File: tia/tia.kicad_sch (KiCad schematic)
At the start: 29 parts, among them J1 ToADC, J2 Sensors, U1 Opamp_Quad, U2 Opamp_Quad, U3 MIC5366-2.0YC5-TR

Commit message: board revs, updated README
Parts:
- added C10, C11, C12, C13, C14, C15, C8, C9: 10pF, Capacitor_SMD:C_0805_2012Metric, symbol Device:C_Small
- added C7: 0.01uF X7R, Capacitor_SMD:C_0805_2012Metric, symbol Device:C_Small
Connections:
- net A0N: now also J1.1 (Pin_1), C8.2; no longer J1.2 (Pin_2)
- net A1N: now also J1.3 (Pin_3), C10.2; no longer J1.4 (Pin_4)
- net A2N: now also J1.5 (Pin_5), C12.2; no longer J1.6 (Pin_6)
- net A3N: now also J1.7 (Pin_7), C14.2; no longer J1.8 (Pin_8)
- net A4N: now also J1.9 (Pin_9), C9.2; no longer J1.10 (Pin_10)
- net A5N: now also J1.11 (Pin_11), C11.2; no longer J1.12 (Pin_12)
- net A6N: now also J1.13 (Pin_13), C13.2; no longer J1.14 (Pin_14)
- net A7N: now also J1.15 (Pin_15), C15.2; no longer J1.16 (Pin_16)
- net GND: now also J1.18 (Pin_18), J1.20 (Pin_20), C7.2; no longer J1.17 (Pin_17), J1.19 (Pin_19)
- net S0: now also C8.1
- net S1: now also C10.1
- net S2: now also C12.1
- net S3: now also C14.1
- net S4: now also C9.1
- net S5: now also C11.1
- net S6: now also C13.1
- net S7: now also C15.1
- net VAA: now also J1.19 (Pin_19); no longer J1.20 (Pin_20)
- net VREF: now also J1.10 (Pin_10), J1.12 (Pin_12), J1.14 (Pin_14), J1.16 (Pin_16), J1.17 (Pin_17), J1.2 (Pin_2), J1.4 (Pin_4), J1.6 (Pin_6), J1.8 (Pin_8); no longer J1.1 (Pin_1), J1.11 (Pin_11), J1.13 (Pin_13), J1.15 (Pin_15), J1.18 (Pin_18), J1.3 (Pin_3), J1.5 (Pin_5), J1.7 (Pin_7), J1.9 (Pin_9)
- net at U3.4 (BYP): now also C7.1
- no-connect marks 1 -> 0
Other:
- note added: "Also: REF3312AIDCKR 1.25V, lower noise $1.76/ea @ 10 NOT COMPATIBLE"
- note added: "Also: TPS717 is compatible, and can use the bypass cap"
- note removed: "Also: REF3312AIDCKR 1.25V, lower noise $1.76/ea @ 10"
- moved on the sheet: C1, C6, H1, H2, J2, R1, R2, R3, R4, R5, R6, R7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

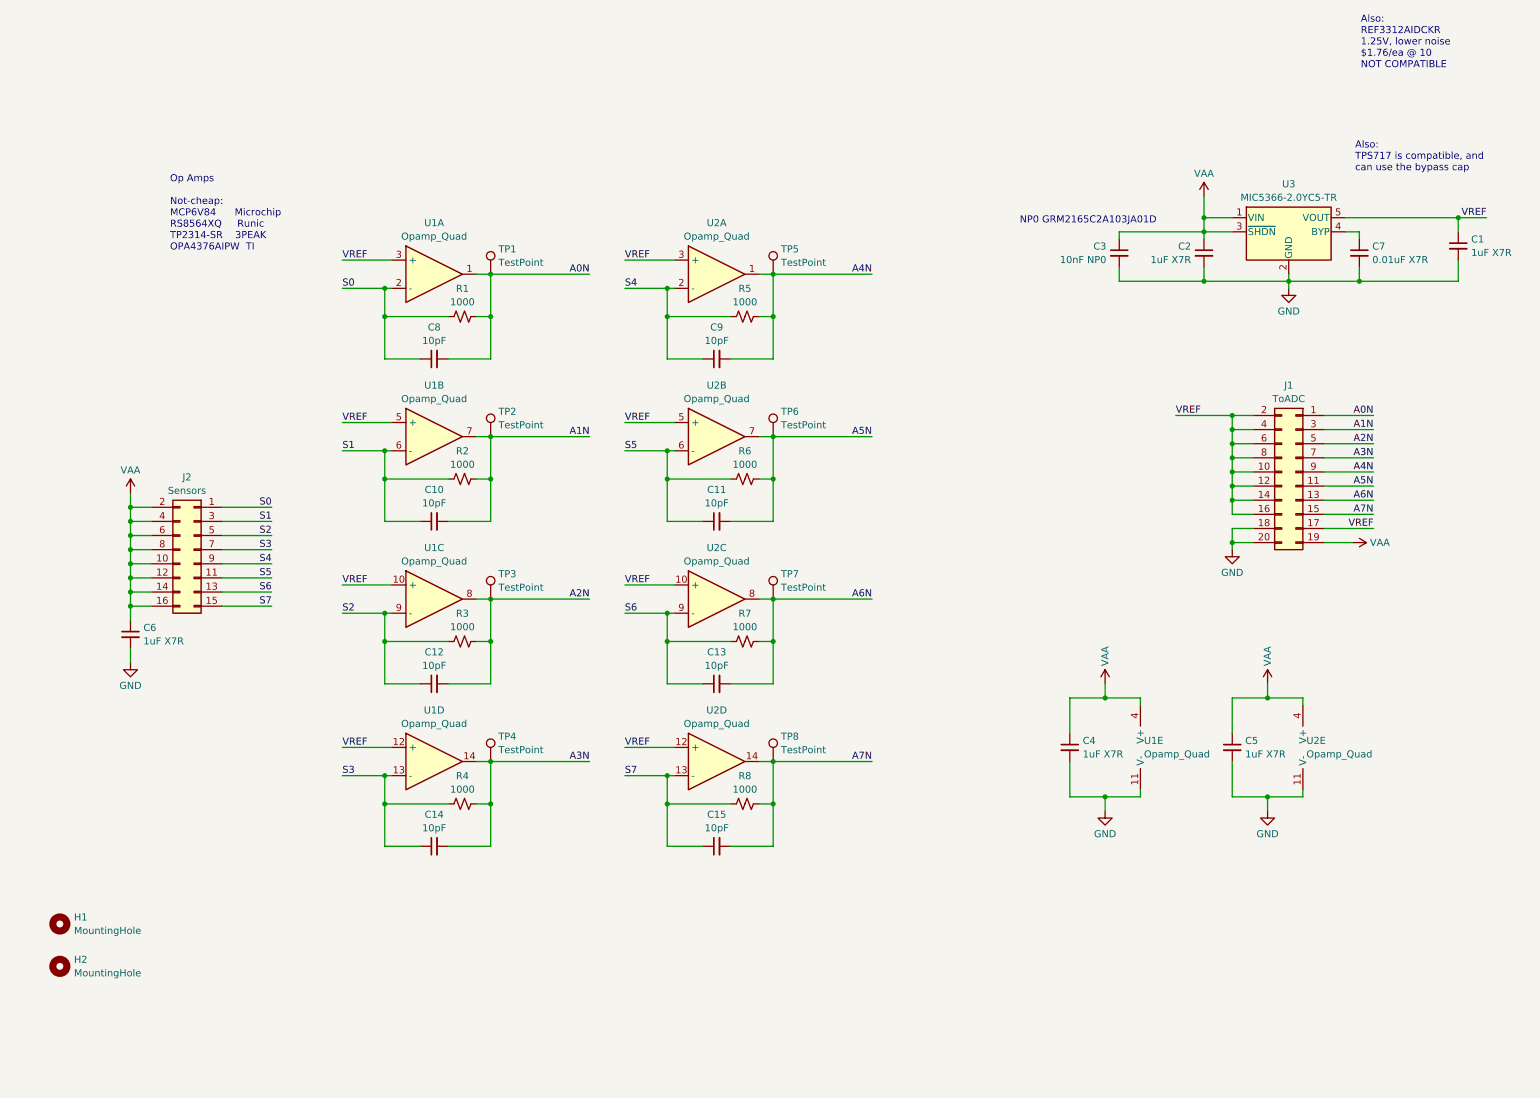
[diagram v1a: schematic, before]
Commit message: rev2 of tia board, with bias and LPF
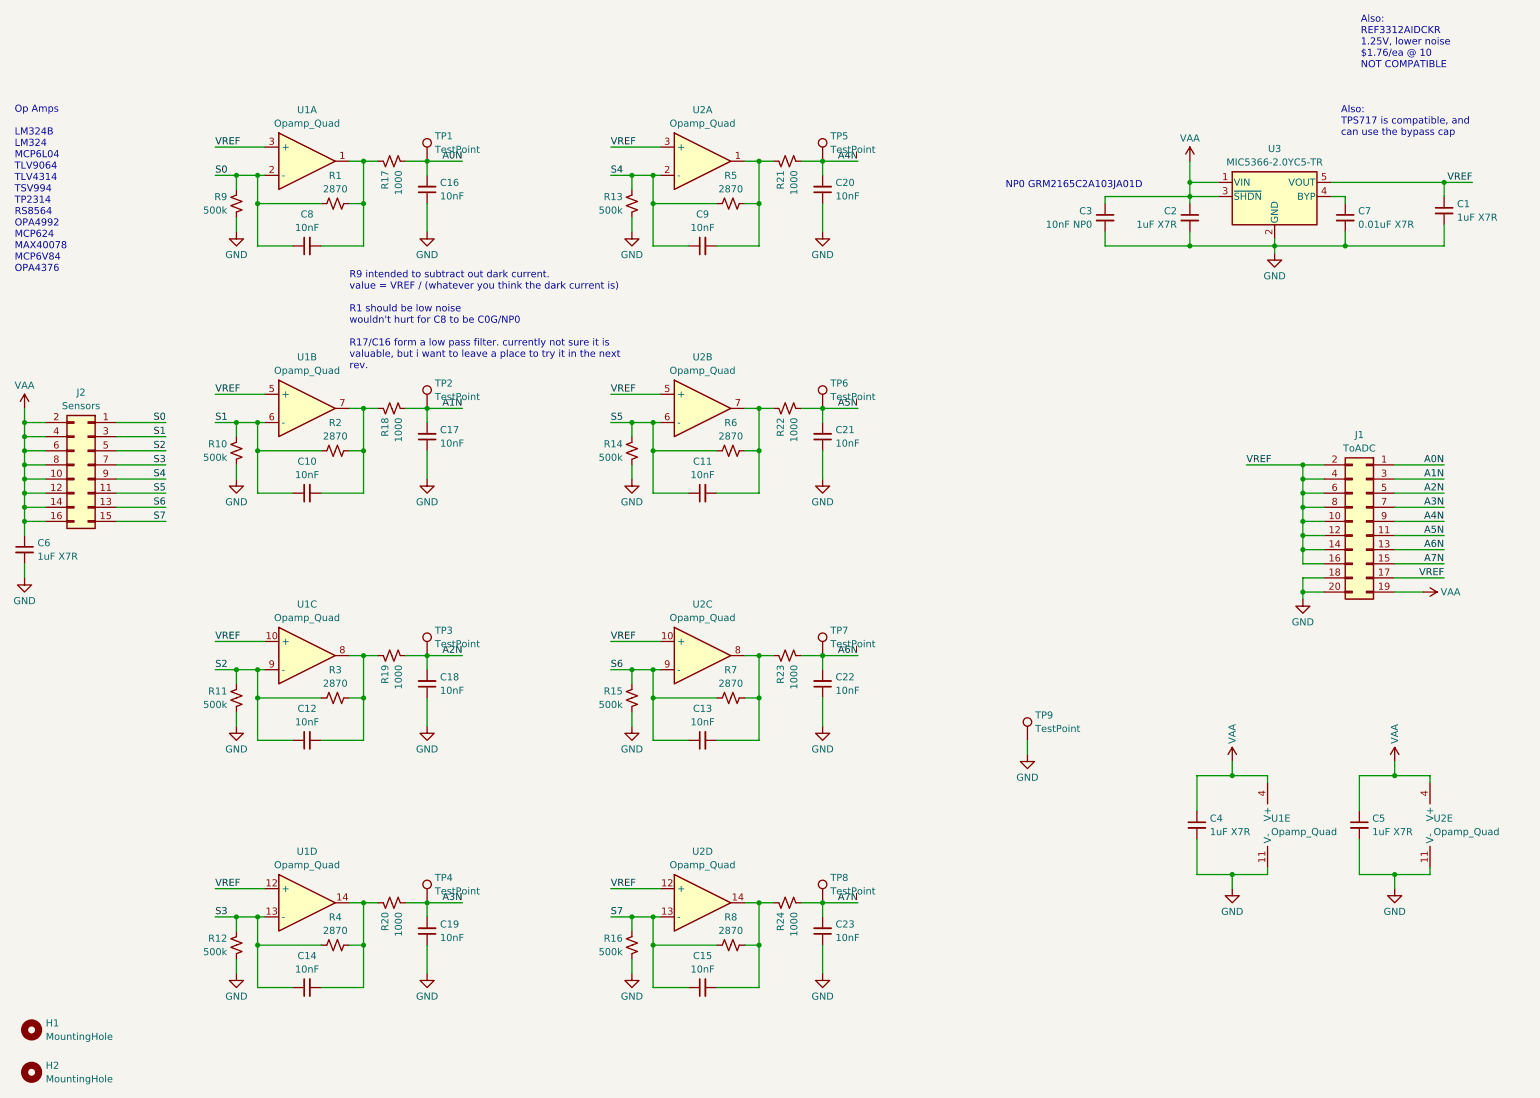
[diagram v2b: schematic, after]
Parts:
- added C16, C17, C18, C19, C20, C21, C22, C23: 10nF, Capacitor_SMD:C_0805_2012Metric, symbol Device:C_Small
- added R10, R11, R12, R13, R14, R15, R16, R9: 500k, Resistor_SMD:R_0805_2012Metric, symbol Device:R_Small_US
- added R17, R18, R19, R20, R21, R22, R23, R24: 1000, Resistor_SMD:R_0805_2012Metric, symbol Device:R_Small_US
- added TP9: TestPoint, TestPoint:TestPoint_Pad_D2.0mm, symbol Connector:TestPoint
- C10, C11, C12, C13, C14, C15, C8, C9: value 10pF -> 10nF
- R1, R2, R3, R4, R5, R6, R7, R8: value 1000 -> 2870
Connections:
- net A0N: now also C16.2, R17.1; no longer C8.2, R1.2, U1.1
- net A1N: now also C17.2, R18.1; no longer C10.2, R2.2, U1.7
- net A2N: now also C18.2, R19.1; no longer C12.2, R3.2, U1.8
- net A3N: now also C19.2, R20.1; no longer C14.2, R4.2, U1.14
- net A4N: now also C20.2, R21.1; no longer C9.2, R5.2, U2.1
- net A5N: now also C21.2, R22.1; no longer C11.2, R6.2, U2.7
- net A6N: now also C22.2, R23.1; no longer C13.2, R7.2, U2.8
- net A7N: now also C23.2, R24.1; no longer C15.2, R8.2, U2.14
- net GND: now also C16.1, C17.1, C18.1, C19.1, C20.1, C21.1, C22.1, C23.1, R10.1, R11.1, R12.1, R13.1, R14.1, R15.1, R16.1, R9.1, TP9.1
- net S0: now also R9.2
- net S1: now also R10.2
- net S2: now also R11.2
- net S3: now also R12.2
- net S4: now also R13.2
- net S5: now also R14.2
- net S6: now also R15.2
- net S7: now also R16.2
- new net: C15.2, R24.2, R8.2, U2.14
- new net: C13.2, R23.2, R7.2, U2.8
- new net: C9.2, R21.2, R5.2, U2.1
- new net: C8.2, R1.2, R17.2, U1.1
- new net: C11.2, R22.2, R6.2, U2.7
- new net: C14.2, R20.2, R4.2, U1.14
- new net: C10.2, R18.2, R2.2, U1.7
- new net: C12.2, R19.2, R3.2, U1.8
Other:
- note added: "Op Amps LM324B LM324 MCP6L04 TLV9064 TLV4314 TSV994 TP2314 RS8564 OPA4992 MCP624 MAX40078 MCP6V84 OPA4376"
- note added: "R9 intended to subtract out dark current. value = VREF / (whatever you think the dark current is) R1 should be low noise wouldn't hurt for C8 to be C0G/NP0 R17/C16 form a low pass filter. currently not sure it is valuable, but i want to leave a place to try it in the next rev."
- note removed: "Op Amps Not-cheap: MCP6V84 Microchip RS8564XQ Runic TP2314-SR 3PEAK OPA4376AIPW TI"
- moved on the sheet: C1, C10, C11, C12, C13, C14, C15, C2, C3, C4, C5, C6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
